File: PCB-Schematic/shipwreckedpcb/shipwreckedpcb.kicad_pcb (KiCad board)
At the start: 4 copper layers, 61.8 x 79.6 mm, 149 parts, among them J1 USB4105, J14 Conn_01x01, J15 Conn_01x01, J16 Conn_01x01, J17 Conn_01x01, J18 Conn_01x01, J19 Conn_01x01, J2 Waveshare 1.54" E-Ink, J20 Conn_01x01, J21 Conn_01x01, J22 Conn_01x01, J23 Conn_01x01, J24 Conn_01x01, J25 Conn_01x01, J26 Conn_01x01, J28 Conn_01x01, J29 Conn_01x01, J3 Conn_01x01, J30 Conn_01x01, J31 Conn_01x01, J32 Conn_01x01, J33 Conn_01x01, J34 Conn_01x01, J35 Conn_01x01, J36 Conn_01x01, J37 Conn_01x01, J38 Conn_01x01, J39 Conn_01x01, J4 Conn_01x01, J40 Conn_01x01, J5 SWD, J6 Conn_01x01, J7 Conn_01x01, J8 B2B Male, J9 B2B Female, Q1 Si1308EDL, SW1 BOOTSEL, SW10 Clicky - THT, SW11 Clicky - THT, SW12 Clicky - THT, SW13 Clicky - THT, SW14 Clicky - THT, SW15 Clicky - THT, SW16 Clicky - THT, SW17 Clicky - THT, SW18 Clicky - THT, SW19 PWR Switch, SW2 RESET, SW3 Clicky - THT, SW4 Clicky - THT, SW5 Clicky - THT, SW6 Clicky - THT, SW7 Clicky - THT, SW8 Clicky - THT, SW9 Clicky - THT, U1 RP2040, U2 W25Q128JVS, U3 PE4259, U4 TPS61200DRC, U6 AMS1117-3.3, U7 PCA9555PW, U8 SX1262IMLTRT, Y1 ABM8-272-T3, Y2 32MHz

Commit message: silkscreen updates
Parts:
- moved kibuzzard-687865CB 2.17 mm to (165.1, 68.8)
- moved kibuzzard-687864C4 1.03 mm to (134.6, 109.2)
- moved kibuzzard-6878653F 0.65 mm to (129.1, 76.0)
- moved kibuzzard-68786588 0.10 mm to (120.9, 63.8)
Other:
- board text added: "10"
- board text added: "11"
- board text added: "12"
- board text added: "13"
- board text added: "14"
- board text added: "15"
- board text added: "29"
- board text added: "3v3"
- board text added: "5v"
- board text added: "6"
- board text added: "7"
- board text added: "8"
- board text added: "9"
- board text added: "Art by @Ruby PCB and Circuit by Max Kendall Firmware development by River Lewis Assistance from Alex Park and Evan Gan"
- board text added: "CLK"
- board text added: "GND"
- board text added: "MISO"
- board text added: "MOSI"
- board text added: "SCL"
- board text added: "SDA"
- board text removed: "PCB and Circuit by Max Kendall Firmware development by River Lewis Assistance from Alex Park and Evan Gan"

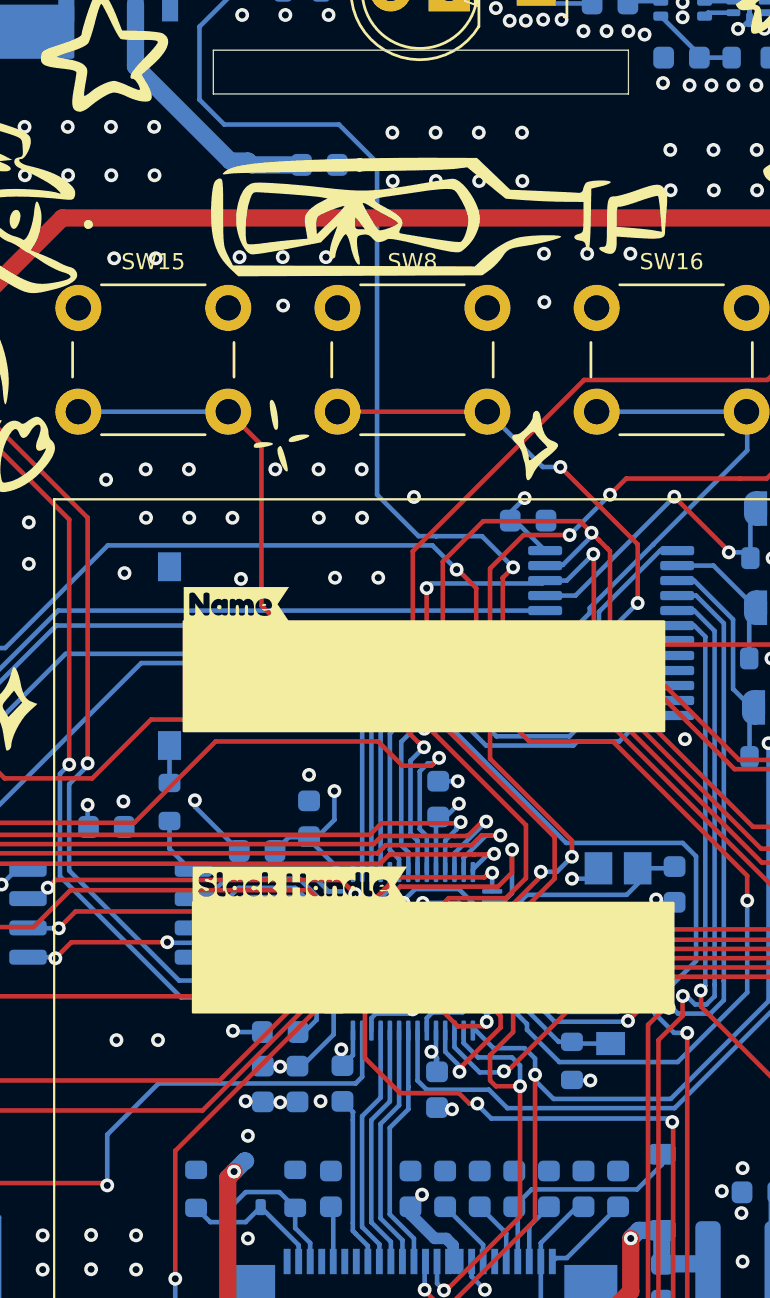
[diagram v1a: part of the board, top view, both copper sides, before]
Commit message: if i didn't click update pcb from schematic i wouldn't have noticed i deleted the battery
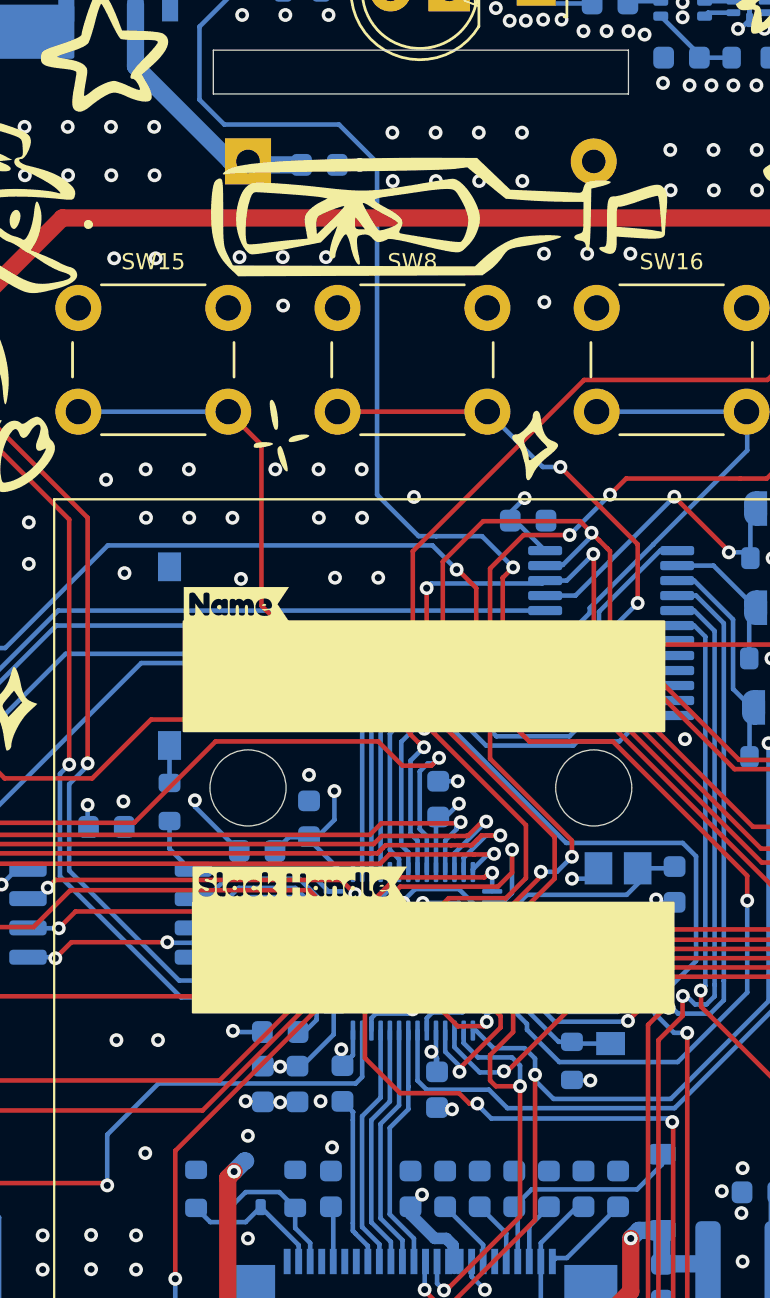
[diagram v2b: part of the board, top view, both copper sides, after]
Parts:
- added BT1: 2x AA, Battery:BatteryHolder_Keystone_2462_2xAA, B.Cu at (139.6, 72.4)
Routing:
- net Earth: vias 238 -> 240

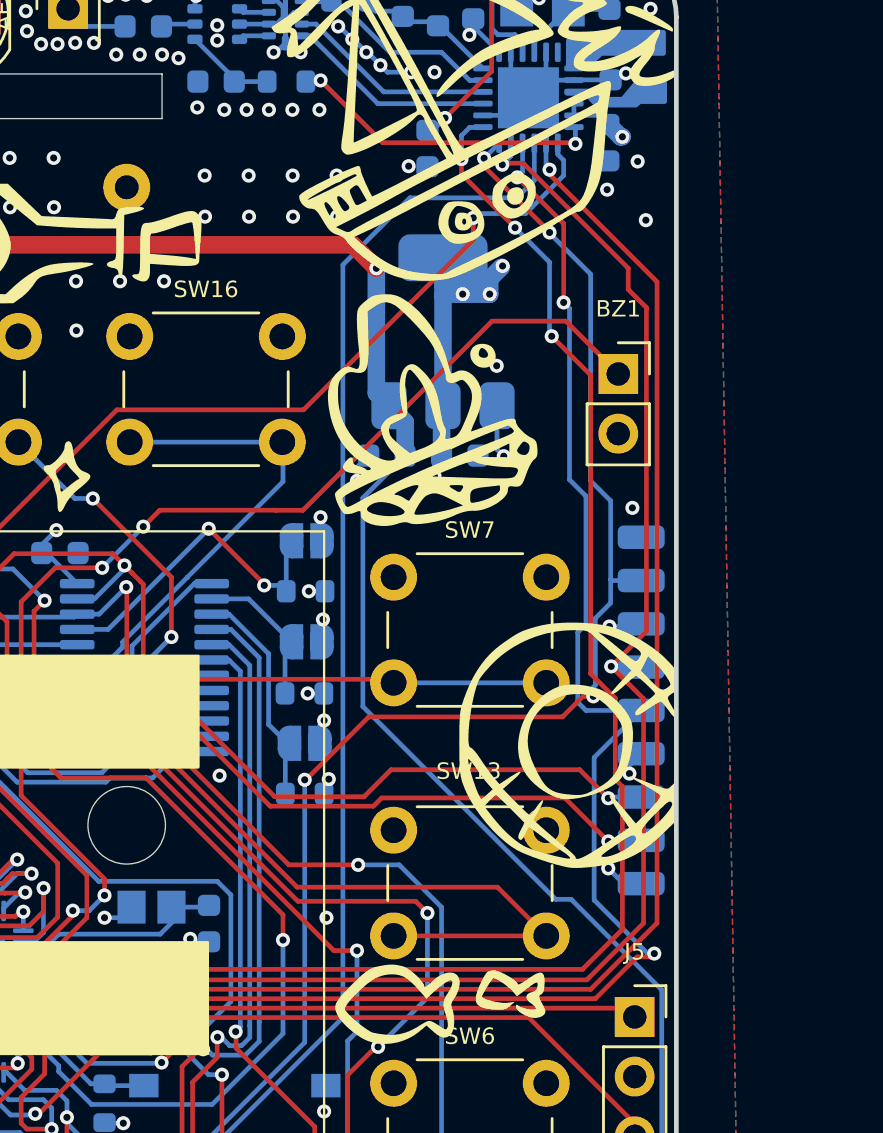
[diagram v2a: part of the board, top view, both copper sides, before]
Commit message: bom and buzzer
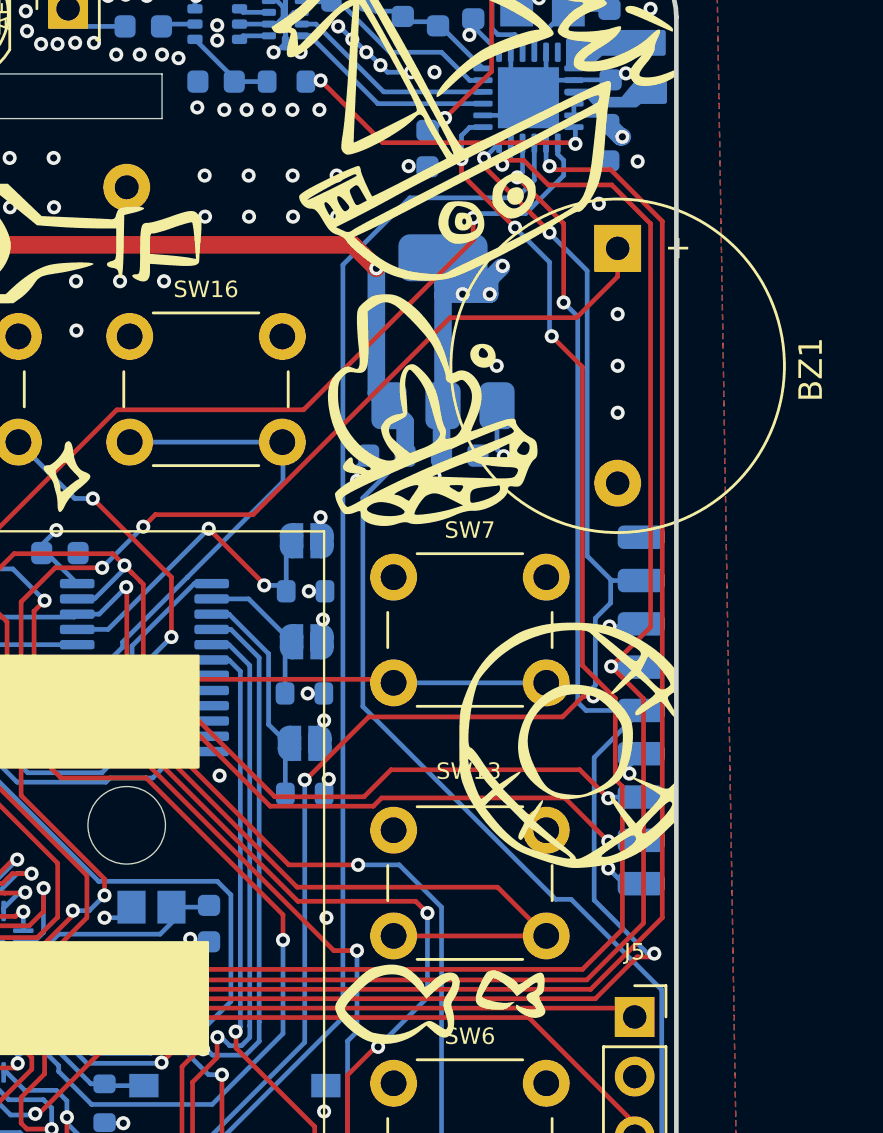
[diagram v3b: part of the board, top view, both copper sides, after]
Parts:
- removed kibuzzard-687865EC: G***, kibuzzard-687865EC
- added kibuzzard-687ADB8B: G***, kibuzzard-687ADB8B, B.Cu at (160.0, 76.9)
- BZ1: footprint Connector_PinSocket_2.54mm:PinSocket_1x02_P2.54mm_Vertical -> Buzzer_Beeper:Buzzer_D14mm_H7mm_P10mm
- moved BZ1 5.35 mm to (175.4, 75.0), turned to -90 degrees
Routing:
- net /SPI_MOSI: track 92.7 -> 94.6 mm
- net /SX_BUSY: track 68.5 -> 70.1 mm
- net /GPIO28_ADC2_BUZZER: track 58.3 -> 59.3 mm
- net Earth: vias 240 -> 241
